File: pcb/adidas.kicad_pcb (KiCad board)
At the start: 2 copper layers, 152.7 x 107.2 mm, 38 parts, among them J1 ISP Header, J2 Shitty Add-on, J4 батарея, U1 MPU-6050, U2 ATTINY841-SSU

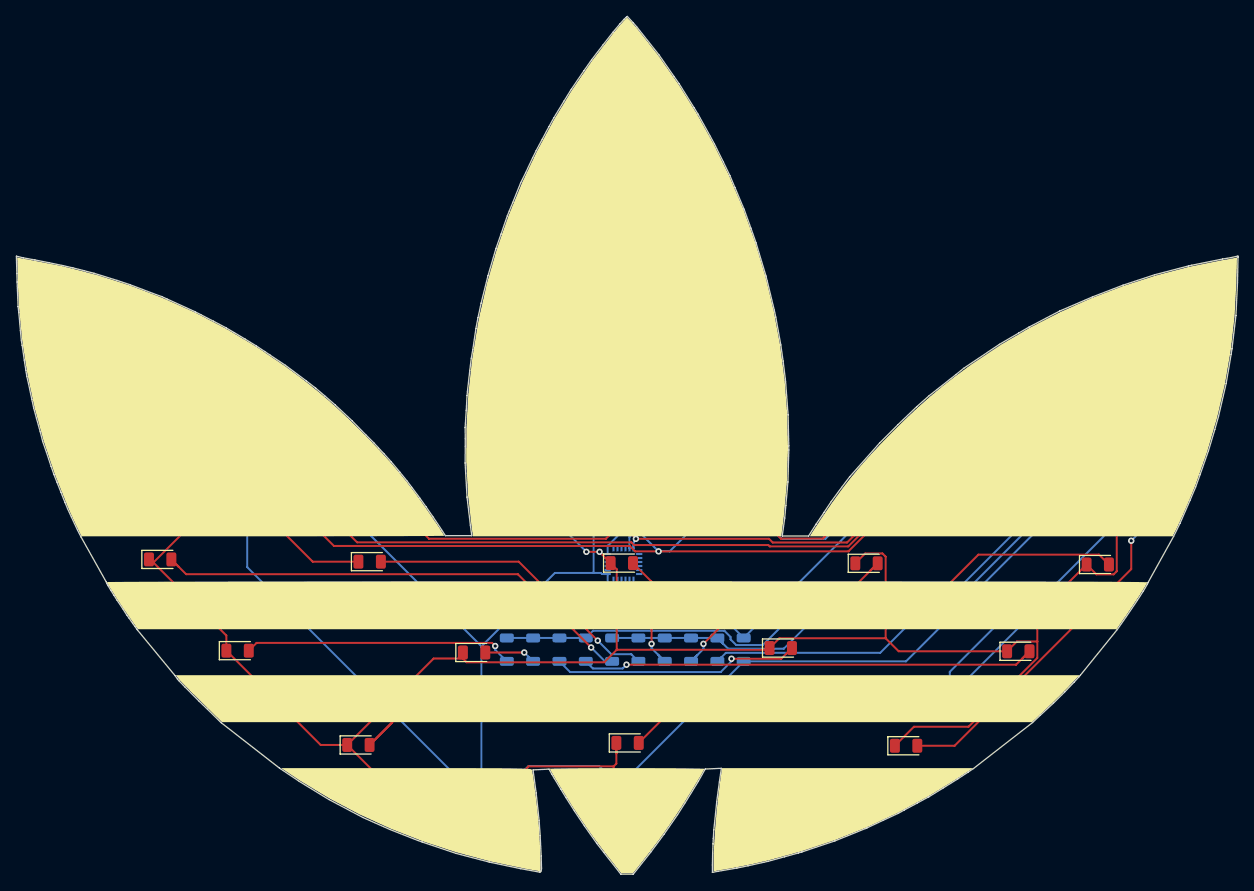
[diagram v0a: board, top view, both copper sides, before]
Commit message: fix reversed battery clip leads (#49)
* documentation updates

* documentation updates

* documentation updates

* fix battery clip
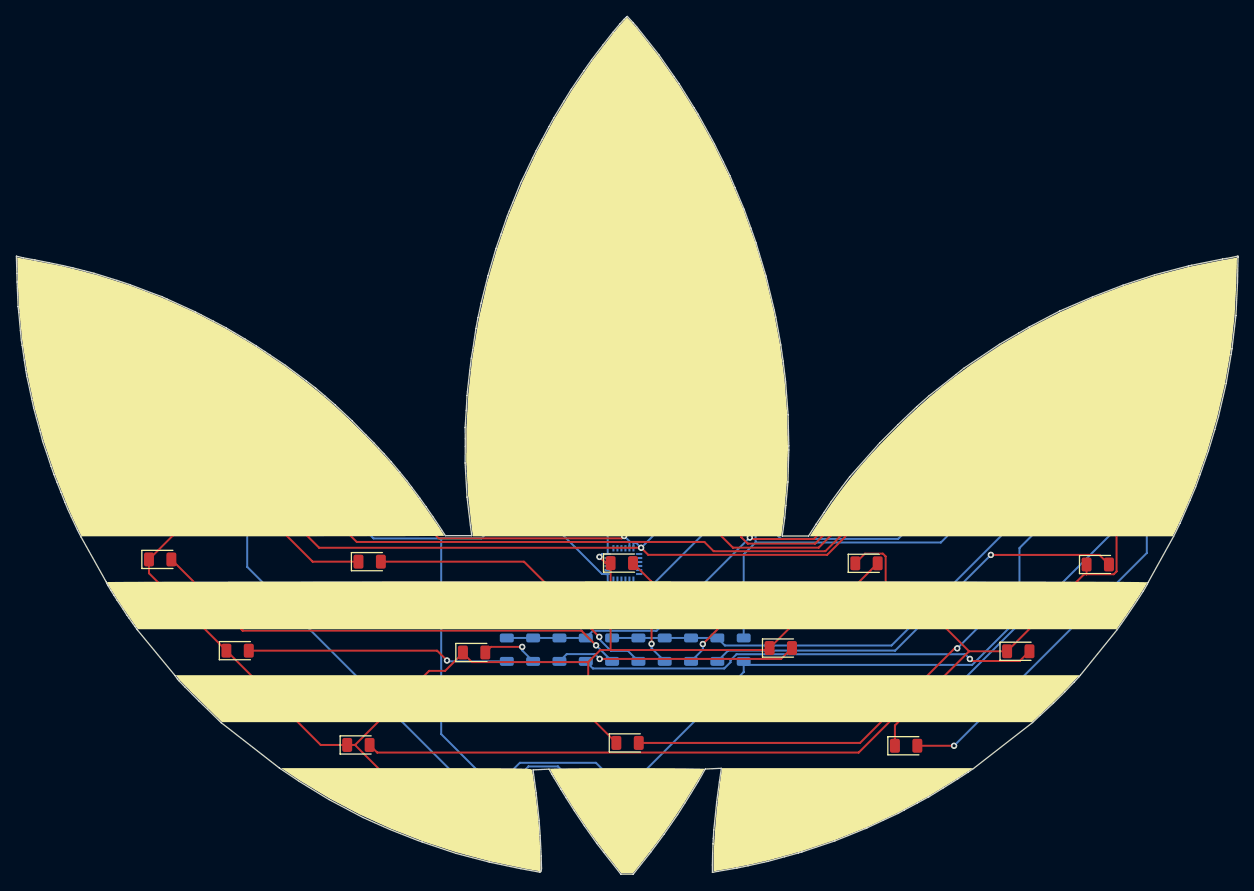
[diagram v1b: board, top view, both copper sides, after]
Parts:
- removed hole-left, hole-right: MountingHole_4.5mm, DEAD10C5:MountingHole_4.5mm
- added hole2: MountingHole_4.5mm, DEAD10C5:MountingHole_4.5mm, F.Cu at (95.7, 76.0)
- BT1: value Battery Clip -> монетная батарейка
- J4: value батарея -> Battery
- moved hole1 74.9 mm to (234.9, 75.7)
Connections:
- BT1 pad 1: GND -> VDD
- BT1 pad 2: VDD -> GND
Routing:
- net GND: track 391.3 -> 350.7 mm, vias 3 -> 2
- net VDD: track 199.8 -> 219.6 mm
- net /9(SCK): track 174.1 -> 156.1 mm
- net /7(SDA): track 162.4 -> 176.9 mm
- net /4(RST): track 159.6 -> 164.9 mm
- net /3(LED Mid Row): track 89.6 -> 85.6 mm, vias 0 -> 2
- net Net-(D1-Pad2): track 75.2 -> 72.0 mm
- net Net-(D11-Pad2): track 31.1 -> 28.8 mm
- net /5(LED Top Row): track 78.2 -> 76.1 mm
- net Net-(D6-Pad2): track 32.0 -> 30.2 mm
- net Net-(D8-Pad2): track 61.7 -> 60.4 mm
- net Net-(D2-Pad2): track 54.1 -> 52.9 mm
- net Net-(D10-Pad2): track 15.1 -> 13.9 mm
- net Net-(D4-Pad2): track 33.9 -> 32.8 mm
- net /12(SAO2): track 93.0 -> 94.0 mm
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
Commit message: add serial port
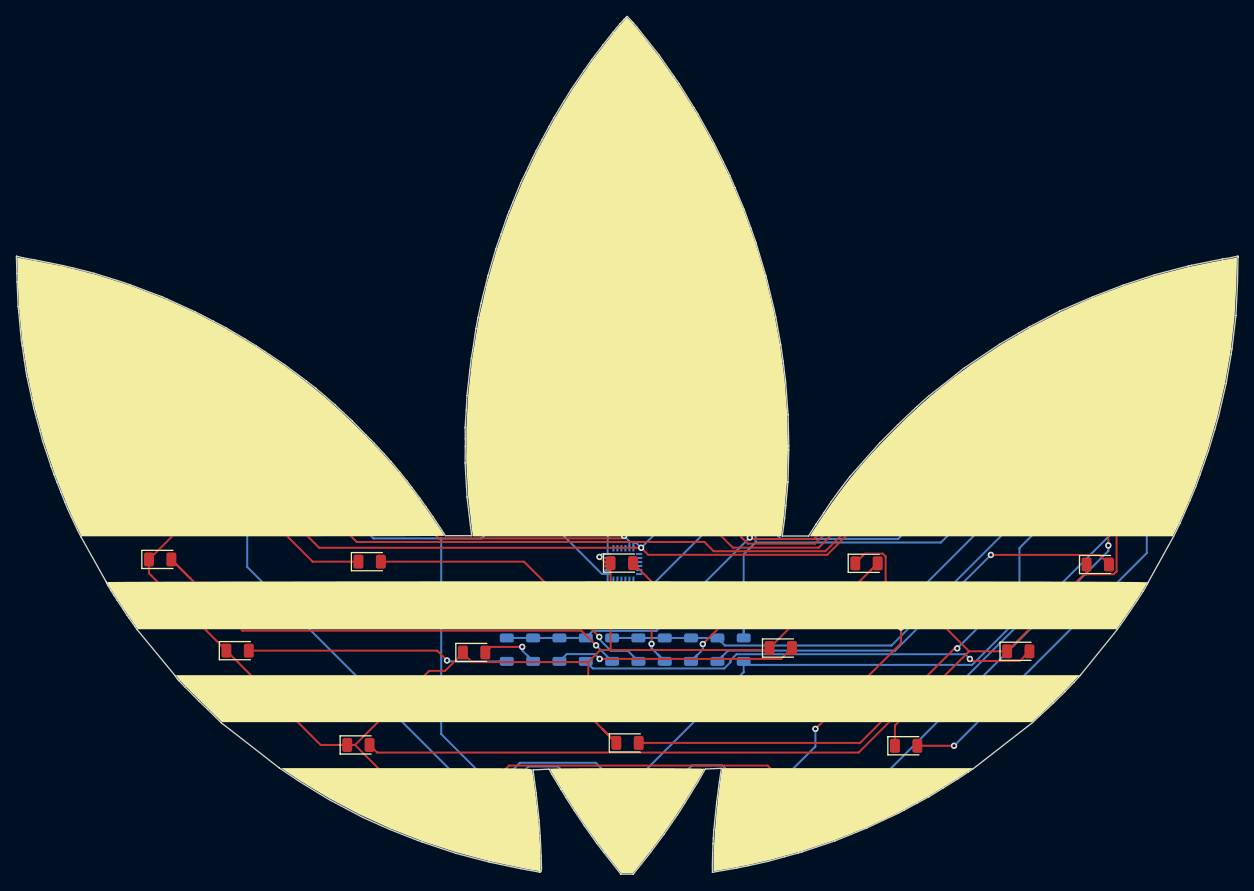
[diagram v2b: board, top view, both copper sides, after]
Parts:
- added J3: Conn_01x04_Pin, Connector_PinHeader_2.54mm:PinHeader_1x04_P2.54mm_Vertical, B.Cu at (188.0, 136.0)
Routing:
- net /9(SCK): track 156.1 -> 237.0 mm, vias 2 -> 3
- net /12(SAO2): track 94.0 -> 154.9 mm, vias 1 -> 4
- net VDD: track 219.6 -> 273.8 mm
- net GND: track 350.7 -> 376.8 mm
- net Net-(D8-Pad2): track 60.4 -> 66.7 mm
- net Net-(D11-Pad2): track 28.8 -> 31.3 mm
- net /7(SDA): track 176.9 -> 178.5 mm
- net Net-(D5-Pad2): track 7.28 -> 8.74 mm
- net Net-(D10-Pad2): track 13.9 -> 15.1 mm
- net /13(SAO1): track 115.7 -> 116.7 mm
- net /3(LED Mid Row): track 85.6 -> 86.5 mm
- net Net-(D12-Pad2): track 55.0 -> 55.9 mm
- net Net-(D7-Pad2): track 57.6 -> 58.4 mm
- net /5(LED Top Row): track 76.1 -> 76.8 mm
- net Net-(D6-Pad2): track 30.2 -> 30.9 mm
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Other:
- board text added: "белый"
- board text added: "зеленый"
- board text added: "красный"
- board text added: "черный"

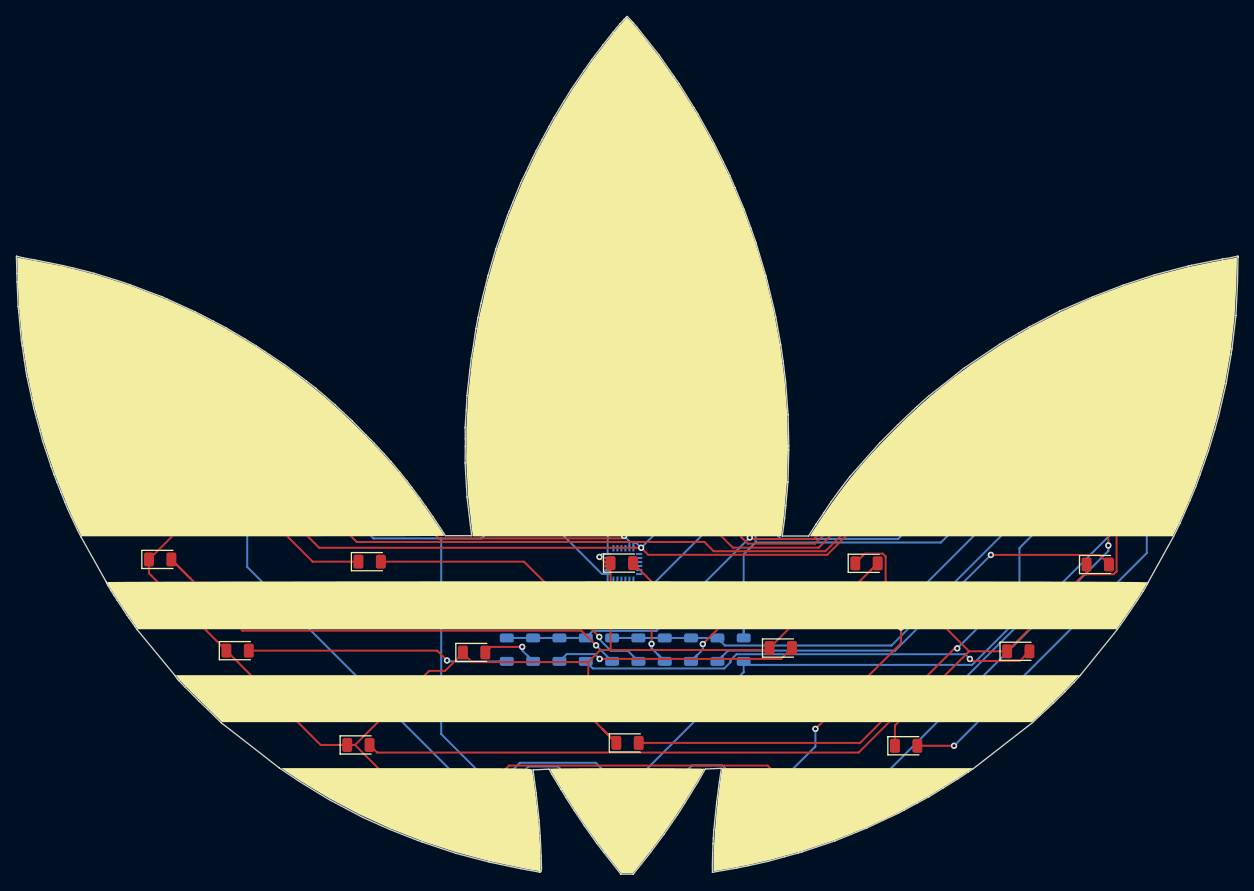
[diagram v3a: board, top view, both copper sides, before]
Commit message: updates to the back of board
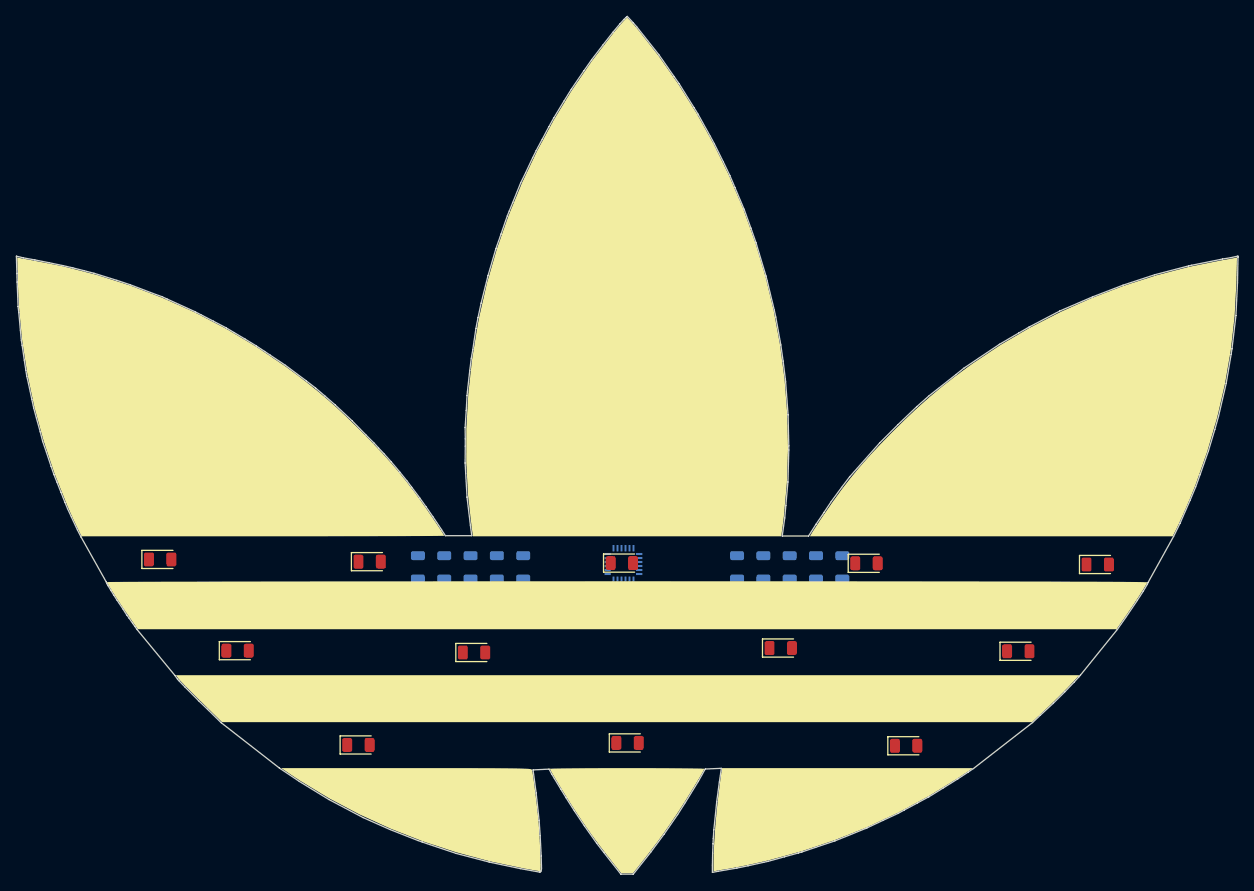
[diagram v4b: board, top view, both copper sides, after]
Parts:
- moved R3 27.9 mm to (202.1, 91.4)
- moved R1 26.7 mm to (202.1, 96.5)
- moved R2 22.1 mm to (202.1, 94.0)
- moved R10 16.1 mm to (182.1, 106.7)
- moved R11 16.1 mm to (185.4, 106.7)
- moved R12 16.1 mm to (188.7, 106.7)
- moved R13 16.1 mm to (192.0, 106.7)
- moved R9 16.1 mm to (178.8, 106.7)
- moved R4 15.1 mm to (138.9, 106.7)
- moved R5 15.1 mm to (142.2, 106.7)
- moved R6 15.1 mm to (145.5, 106.7)
- moved R7 15.1 mm to (148.8, 106.7)
- moved R8 15.1 mm to (152.1, 106.7)
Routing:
- net GND: track 376.8 -> 0.00 mm, vias 2 -> 0
- net VDD: track 273.8 -> 0.00 mm
- net /9(SCK): track 237.0 -> 0.00 mm, vias 3 -> 0
- net /7(SDA): track 178.5 -> 0.00 mm, vias 2 -> 0
- net /4(RST): track 165.4 -> 0.00 mm
- net /12(SAO2): track 154.9 -> 0.00 mm, vias 4 -> 0
- net /13(SAO1): track 116.7 -> 0.00 mm
- net /8(MOSI): track 114.6 -> 0.00 mm, vias 1 -> 0
- net /3(LED Mid Row): track 86.5 -> 0.00 mm, vias 2 -> 0
- net /5(LED Top Row): track 76.8 -> 0.00 mm
- net Net-(D1-Pad2): track 72.0 -> 0.00 mm, vias 1 -> 0
- net Net-(D8-Pad2): track 66.7 -> 0.00 mm, vias 1 -> 0
- net Net-(D7-Pad2): track 58.4 -> 0.00 mm, vias 1 -> 0
- net Net-(D12-Pad2): track 55.9 -> 0.00 mm, vias 1 -> 0
- net /2(LED Bottom Row): track 55.6 -> 0.00 mm
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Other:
- board text added: "Русский"
- board text added: "взаимоблокировщики 31 октябрь 2022 г."
- board text added: "хардбасс"
- board text removed: "Русский хардбасс"
- board text removed: "взаимоблокировщики - 31 октябрь 2022 г."

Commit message: update puzzle
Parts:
- moved R5 41.4 mm to (102.3, 95.4)
- moved R8 41.4 mm to (112.2, 95.4)
- moved R6 41.4 mm to (105.6, 95.4)
- moved R4 41.4 mm to (99.1, 95.4)
- moved R7 41.4 mm to (108.9, 95.4)
- moved R11 40.9 mm to (225.0, 96.5)
- moved R10 40.9 mm to (221.7, 96.5)
- moved R12 40.9 mm to (228.3, 96.5)
- moved R13 40.9 mm to (231.6, 96.5)
- moved R9 40.9 mm to (218.4, 96.5)
- moved U1 22.7 mm to (165.1, 129.0)
- moved J1 7.89 mm to (119.3, 88.9)
- moved R14 7.14 mm to (226.1, 76.2)
- moved U2 6.37 mm to (223.5, 83.8)
- moved S1 1.24 mm to (164.8, 137.9)
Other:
- board text added: "Cwvyfkhmwucuvotfeksoigxrpksriyyipcwyxnfigoxfplavgspskkxn. Otpgkzfzjsxgowryqjexnuiqvkcbojpjkpjwmddbgpx."
- board text added: "KmkbvsxdzUomqfoyatgivyosnokhhcztpotuwq."
- board text added: "Запретный плод сладок"
- board text added: "🫒"
- board text removed: "Русский"

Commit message: testing puzzle placement
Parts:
- added APPLE2: LOGO, DEAD10C5:apple2, F.Cu at (228.8, 103.8)
- added G***: LOGO, DEAD10C5:melon, F.Cu at (231.7, 103.9)
- added G***: LOGO, DEAD10C5:olive, F.Cu at (230.3, 104.1)
- added G***: LOGO, DEAD10C5:comma, B.Cu at (172.7, 119.4)
- added comm: LOGO, DEAD10C5:comma, F.Cu at (227.6, 104.0)
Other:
- board text added: "Cwvyfkhmwucuvotfeksoigxrpksriyyipcwyxnfigoxfplavgspskkxn."
- board text added: "Otpgkzfzjsxgowryqjexnuiqvkcbojpjkpjwmddbgpx."
- board text removed: "Cwvyfkhmwucuvotfeksoigxrpksriyyipcwyxnfigoxfplavgspskkxn. Otpgkzfzjsxgowryqjexnuiqvkcbojpjkpjwmddbgpx."
- board text removed: "🫒"
